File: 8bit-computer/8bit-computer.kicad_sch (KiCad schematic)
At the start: 26 parts, among them J1 USB_B

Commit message: fixing 8bit-computer schematic
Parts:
- removed C24: 10µF, Capacitor_THT:CP_Radial_D5.0mm_P2.00mm, symbol Device:CP1
- removed D2, D3, D4, D5, D6, D7, D8, D9: RED, LED_THT:LED_D5.0mm, symbol Device:LED_ALT
- added C24: 10µF, Capacitor_THT:CP_Radial_D5.0mm_P2.00mm, symbol Device:C_Polarized
- added D2, D3, D4, D5, D6, D7, D8, D9: RED, symbol Device:LED
- R10, R11, R12, R13, R14, R15, R8, R9: value 10K -> 10k
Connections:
- net A register/BUS_0: now also R15.1, D9.2 (A)
- net A register/BUS_1: now also R14.1, D8.2 (A)
- net A register/BUS_2: now also R13.1, D7.2 (A)
- net A register/BUS_3: now also R12.1, D6.2 (A)
- net A register/BUS_4: now also R11.1, D5.2 (A)
- net A register/BUS_5: now also R10.1, D4.2 (A)
- net A register/BUS_6: now also R9.1, D3.2 (A)
- net A register/BUS_7: now also R8.1, D2.2 (A)
- new net: D7.1 (K), R21.1
- new net: D6.1 (K), R20.1
- new net: D2.1 (K), R16.1
- new net: D8.1 (K), R22.1
- new net: D4.1 (K), R18.1
- new net: D3.1 (K), R17.1
- new net: D5.1 (K), R19.1
- new net: D9.1 (K), R23.1
- new net GND: C24.2, J1.4 (GND), J1.SH (Shield), R10.2, R11.2, R12.2, R13.2, R14.2, R15.2, R16.2, R17.2, R18.2, R19.2, R20.2, R21.2, R22.2, R23.2, R8.2, R9.2
- new net VCC: C24.1, J1.1 (VBUS)

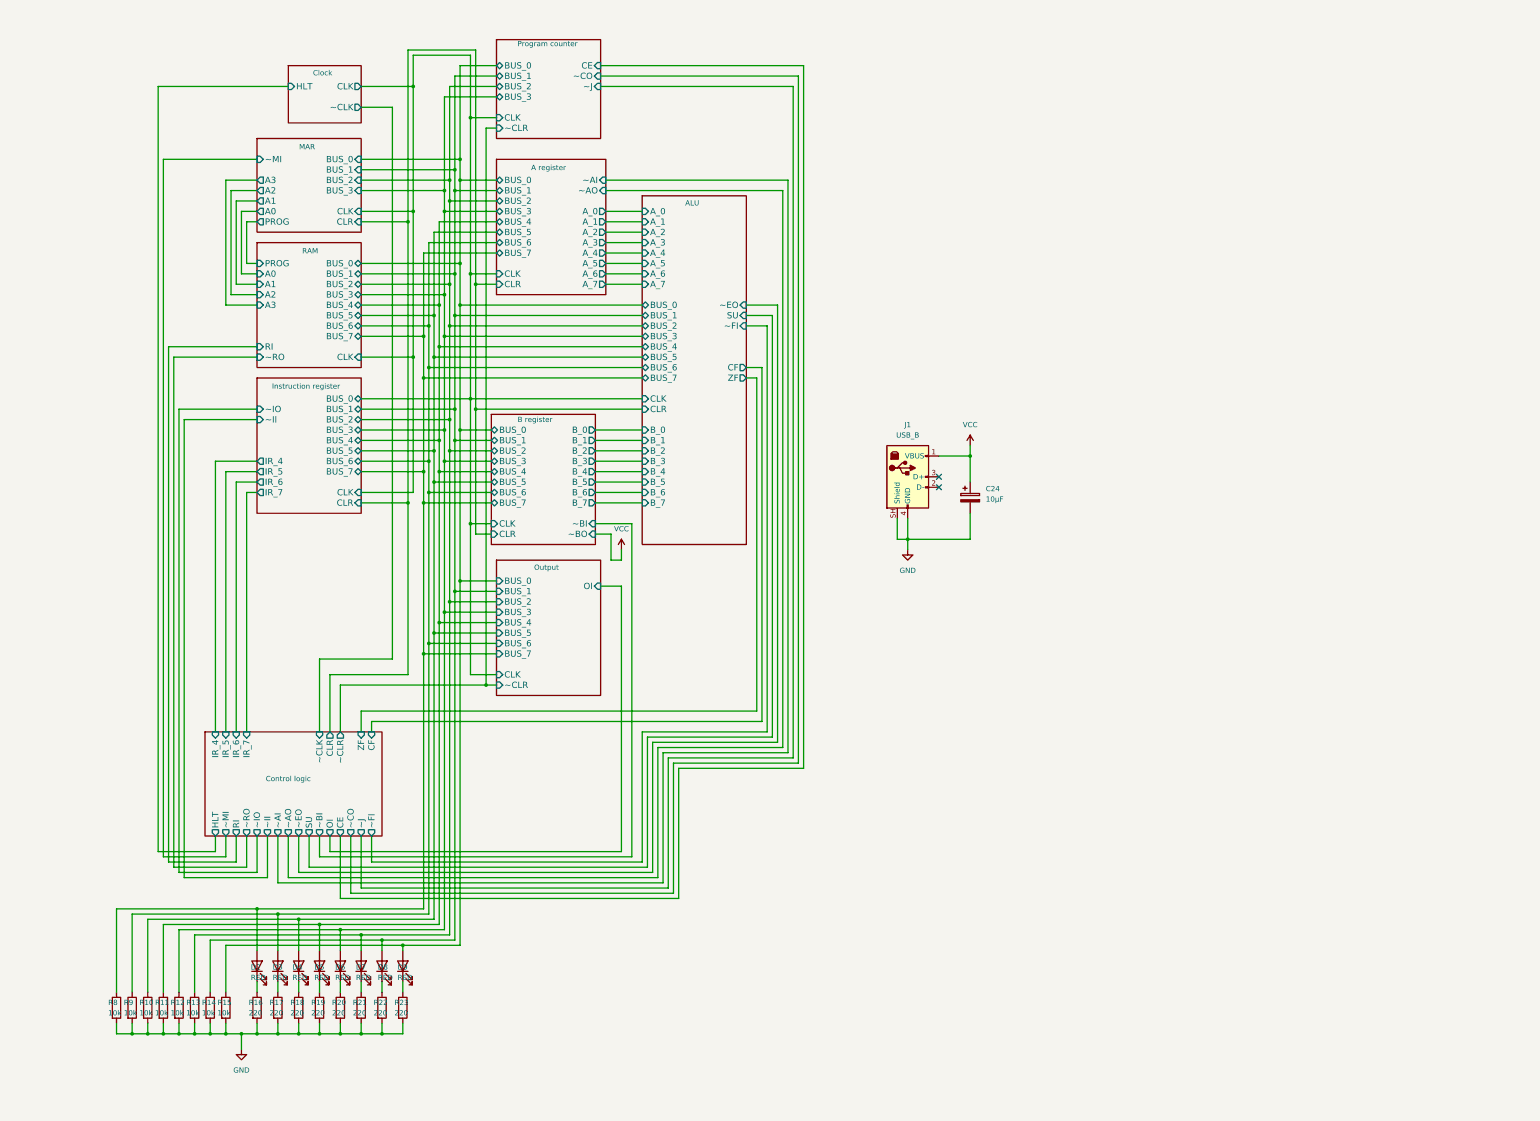
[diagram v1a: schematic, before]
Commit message: cont. drawing CPU
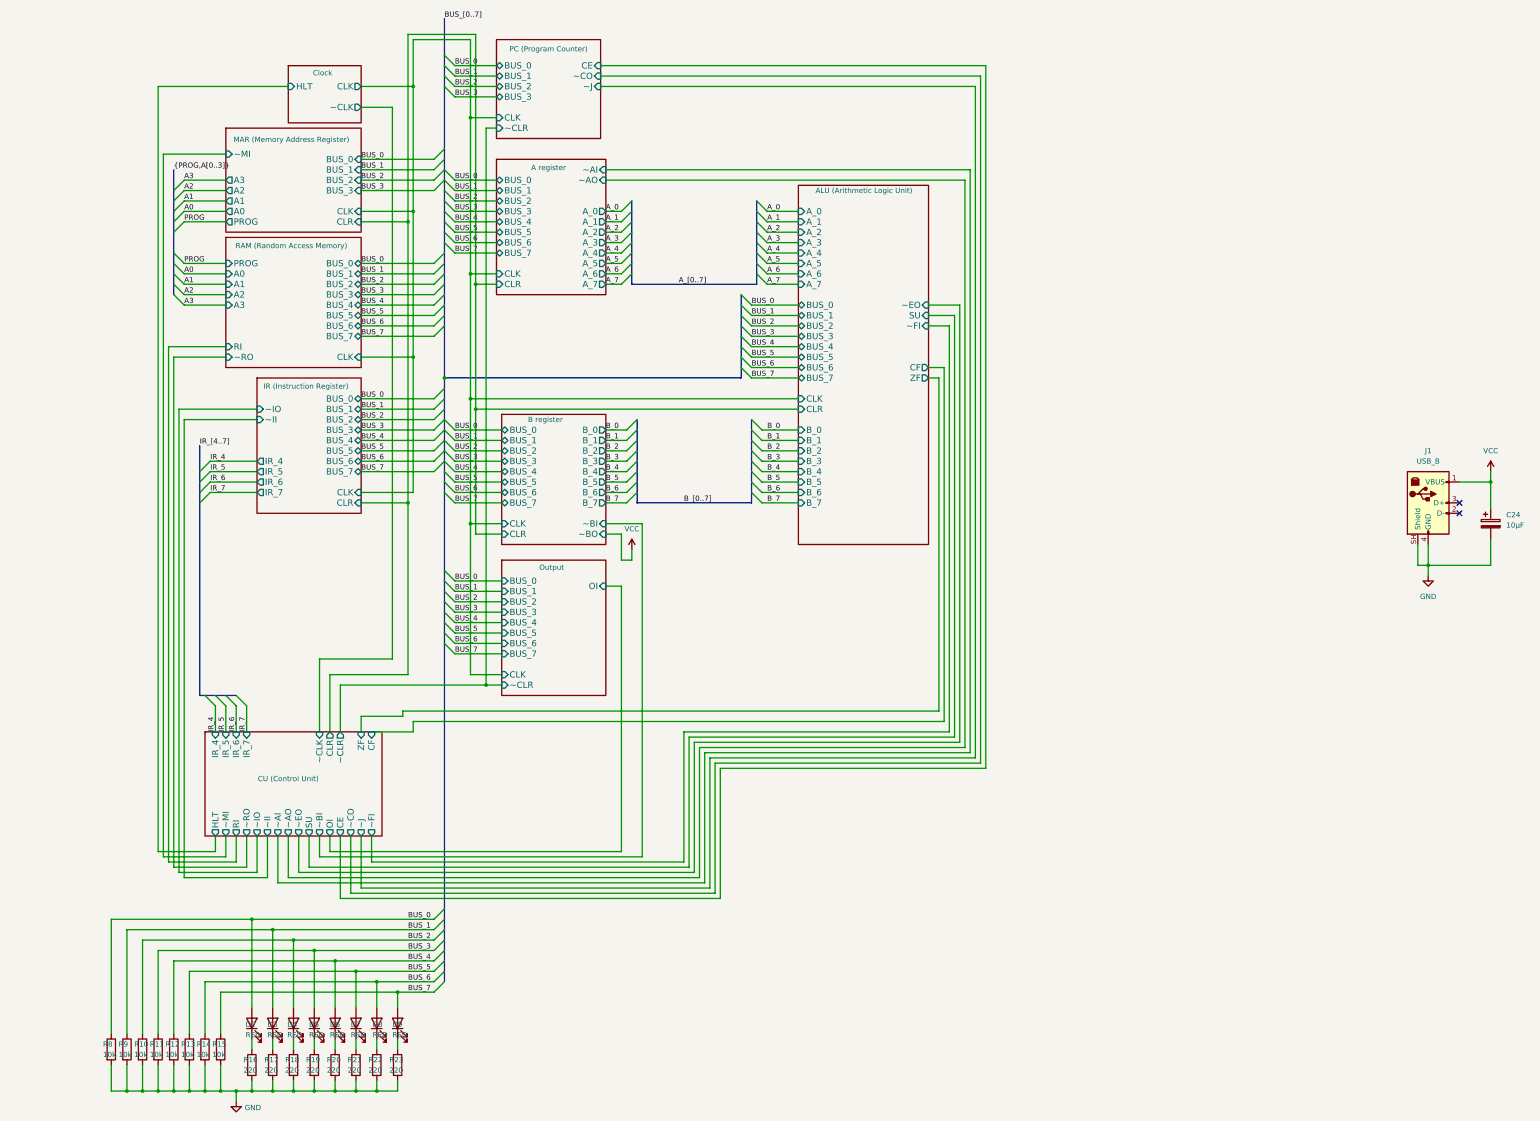
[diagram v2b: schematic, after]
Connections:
- net A register/BUS_0 renamed BUS_7
- net A register/BUS_1 renamed BUS_6
- net A register/BUS_2 renamed BUS_5
- net A register/BUS_3 renamed BUS_4
- net A register/BUS_4 renamed BUS_3
- net A register/BUS_5 renamed BUS_2
- net A register/BUS_6 renamed BUS_1
- net A register/BUS_7 renamed BUS_0
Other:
- sheet ALU renamed ALU (Arithmetic Logic Unit)
- sheet Control logic renamed CU (Control Unit)
- sheet Instruction register renamed IR (Instruction Register)
- sheet MAR renamed MAR (Memory Address Register)
- sheet Program counter renamed PC (Program Counter)
- sheet RAM renamed RAM (Random Access Memory)
- moved on the sheet: C24, D2, D3, D4, D5, D6, D7, D8, D9, J1, R10, R11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

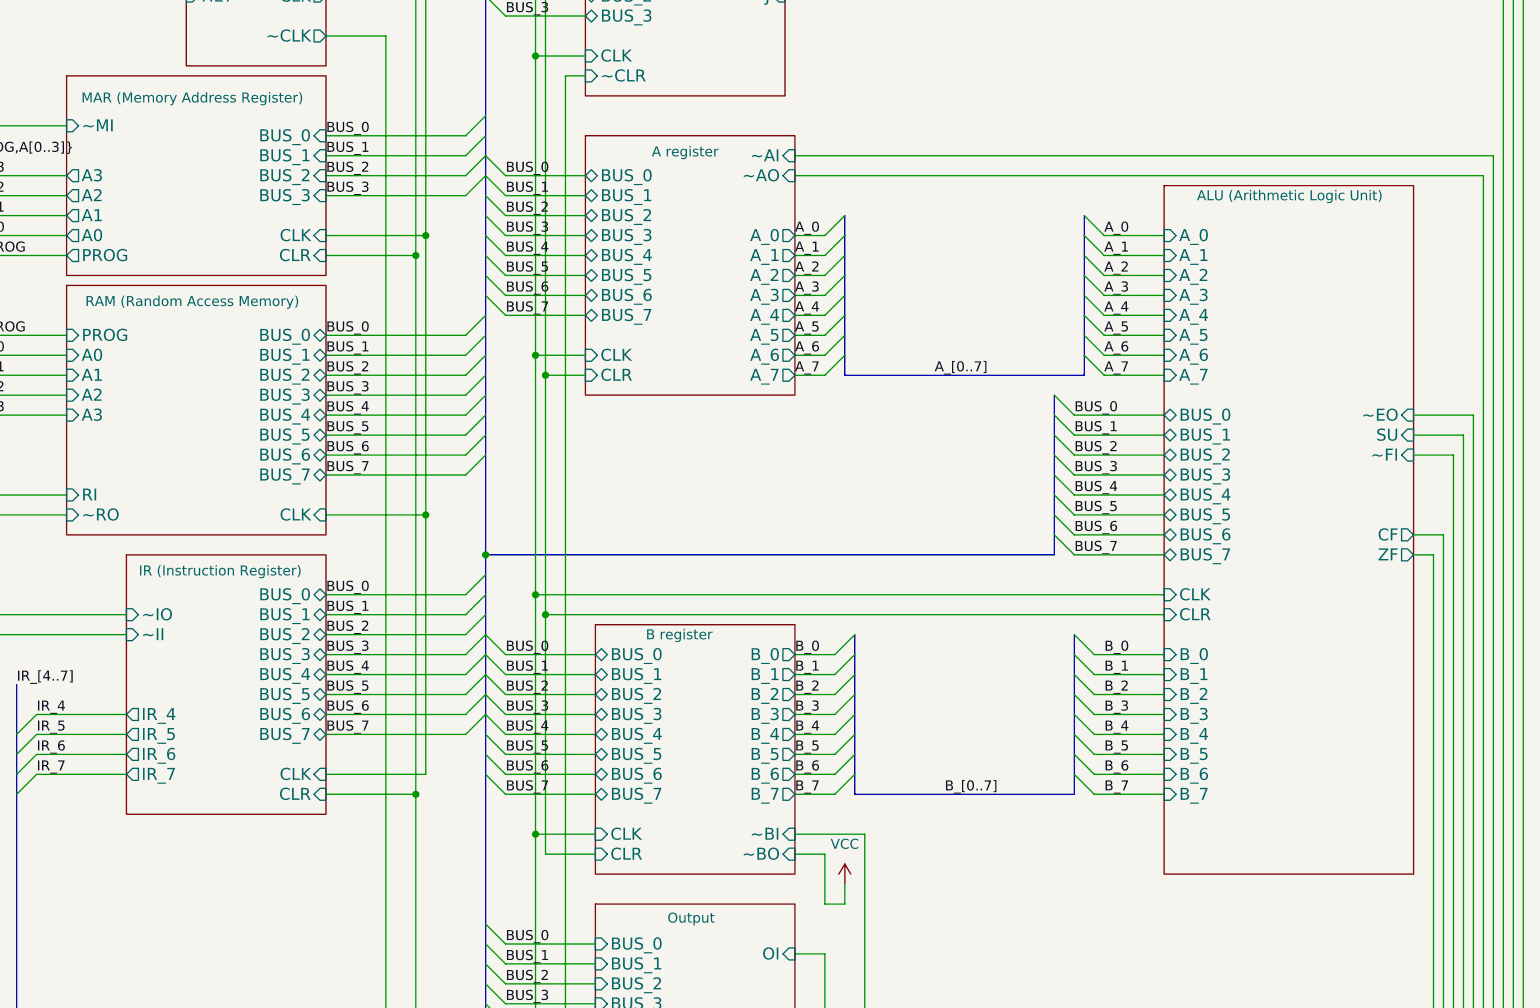
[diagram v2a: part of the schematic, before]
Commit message: using shared register schematic
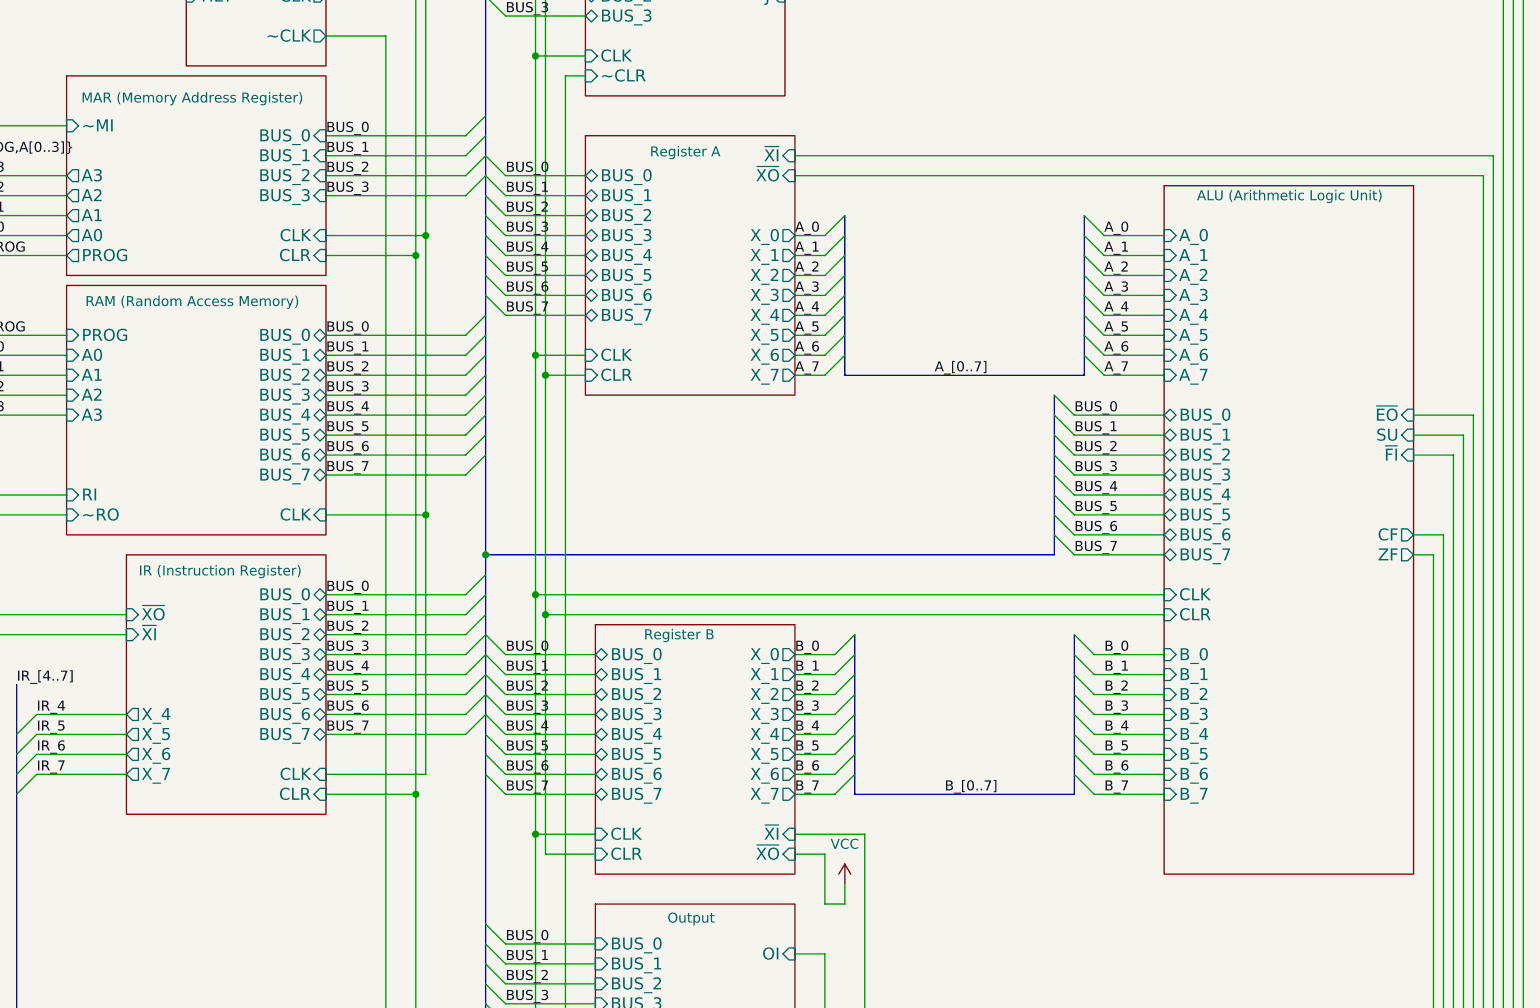
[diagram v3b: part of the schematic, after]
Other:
- sheet A register renamed Register A
- sheet B register renamed Register B
- sheet ALU (Arithmetic Logic Unit) ports: added ~{EO}, ~{FI}; removed ~EO, ~FI
- sheet IR (Instruction Register): file inst-register.kicad_sch -> register.kicad_sch
- sheet IR (Instruction Register) ports: added X_4, X_5, X_6, X_7, ~{XI}, ~{XO}; removed IR_4, IR_5, IR_6, IR_7, ~II, ~IO
- sheet Register A: file a-register.kicad_sch -> register.kicad_sch
- sheet Register A ports: added X_0, X_1, X_2, X_3, X_4, X_5, X_6, X_7, ~{XI}, ~{XO}; removed A_0, A_1, A_2, A_3, A_4, A_5, A_6, A_7, ~AI, ~AO
- sheet Register B: file b-register.kicad_sch -> register.kicad_sch
- sheet Register B ports: added X_0, X_1, X_2, X_3, X_4, X_5, X_6, X_7, ~{XI}, ~{XO}; removed B_0, B_1, B_2, B_3, B_4, B_5, B_6, B_7, ~BI, ~BO
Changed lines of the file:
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@@
 			(color 0 0 0 0)
 		)
-		(property "Sheetname" "B register"
+		(property "Sheetname" "Register B"
 			(at 135.128 113.03 0)
 			(show_name no)
@@
 			)
 		)
-		(property "Sheetfile" "b-register.kicad_sch"
+		(property "Sheetfile" "register.kicad_sch"
 			(at 136.398 115.824 0)
 			(hide yes)
@@
 			)
 		)
-		(pin "B_0" output
+		(pin "X_0" output
 			(at 149.86 115.57 0)
 			(effects
@@
 			)
 		)
-		(pin "B_1" output
+		(pin "X_1" output
 			(at 149.86 118.11 0)
 			(effects
@@
 			)
 		)
-		(pin "B_2" output
+		(pin "X_2" output
 			(at 149.86 120.65 0)
 			(effects
@@
 			)
 		)
-		(pin "B_3" output
+		(pin "X_3" output
 			(at 149.86 123.19 0)
 			(effects
@@
 			)
 		)
-		(pin "B_4" output
+		(pin "X_4" output
 			(at 149.86 125.73 0)
 			(effects
@@
 			)
 		)
-		(pin "B_5" output
+		(pin "X_5" output
 			(at 149.86 128.27 0)
 			(effects
@@
 			)
 		)
-		(pin "B_6" output
+		(pin "X_6" output
 			(at 149.86 130.81 0)
 			(effects
@@
 			)
 		)
-		(pin "B_7" output
+		(pin "X_7" output
 			(at 149.86 133.35 0)
 			(effects
@@
 			)
 		)
-		(pin "~BO" input
+		(pin "~{XO}" input
 			(at 149.86 140.97 0)
 			(effects
@@
 			)
 		)
-		(pin "~BI" input
+		(pin "~{XI}" input
 			(at 149.86 138.43 0)
 			(effects
@@
 			(project "8bit-computer"
 				(path "/ad4ae7b4-c6cb-482b-83a8-8fafb97d09a4"
-					(page "")
+					(page "#")
 				)
 			)
@@
 			(project "8bit-computer"
 				(path "/ad4ae7b4-c6cb-482b-83a8-8fafb97d09a4"
-					(page "")
+					(page "#")
 				)
 			)
@@
 			(project "8bit-computer"
 				(path "/ad4ae7b4-c6cb-482b-83a8-8fafb97d09a4"
-					(page "")
+					(page "#")
 				)
 			)
@@
 			(project "8bit-computer"
 				(path "/ad4ae7b4-c6cb-482b-83a8-8fafb97d09a4"
-					(page "")
+					(page "#")
 				)
 			)
@@
 			)
 		)
-		(property "Sheetfile" "inst-register.kicad_sch"
+		(property "Sheetfile" "register.kicad_sch"
 			(at 76.962 119.38 0)
 			(hide yes)
@@
 			)
 		)
-		(pin "IR_4" output
+		(pin "X_4" output
 			(at 64.77 123.19 180)
 			(effects
@@
 			)
 		)
-		(pin "IR_5" output
+		(pin "X_5" output
 			(at 64.77 125.73 180)
 			(effects
@@
 			)
 		)
-		(pin "IR_6" output
+		(pin "X_6" output
 			(at 64.77 128.27 180)
 			(effects
@@
 			)
 		)
-		(pin "IR_7" output
+		(pin "X_7" output
 			(at 64.77 130.81 180)
 			(effects
@@
 			)
 		)
-		(pin "~IO" input
+		(pin "~{XO}" input
 			(at 64.77 110.49 180)
 			(effects
@@
 			)
 		)
-		(pin "~II" input
+		(pin "~{XI}" input
 			(at 64.77 113.03 180)
 			(effects
@@
 			(project "8bit-computer"
 				(path "/ad4ae7b4-c6cb-482b-83a8-8fafb97d09a4"
-					(page "")
+					(page "#")
 				)
 			)
@@
 			(project "8bit-computer"
 				(path "/ad4ae7b4-c6cb-482b-83a8-8fafb97d09a4"
-					(page "")
+					(page "#")
 				)
 			)
@@
 			(project "8bit-computer"
 				(path "/ad4ae7b4-c6cb-482b-83a8-8fafb97d09a4"
-					(page "")
+					(page "#")
 				)
 			)
@@
 			)
 		)
-		(pin "~EO" input
+		(pin "~{EO}" input
 			(at 228.6 85.09 0)
 			(effects
@@
 			)
 		)
-		(pin "~FI" input
+		(pin "~{FI}" input
 			(at 228.6 90.17 0)
 			(effects
@@
 			(project "8bit-computer"
 				(path "/ad4ae7b4-c6cb-482b-83a8-8fafb97d09a4"
-					(page "")
+					(page "#")
 				)
 			)
@@
 			(project "8bit-computer"
 				(path "/ad4ae7b4-c6cb-482b-83a8-8fafb97d09a4"
-					(page "")
+					(page "#")
 				)
 			)
@@
 			(color 0 0 0 0)
 		)
-		(property "Sheetname" "A register"
+		(property "Sheetname" "Register A"
 			(at 135.89 51.562 0)
 			(show_name no)
@@
 			)
 		)
-		(property "Sheetfile" "a-register.kicad_sch"
+		(property "Sheetfile" "register.kicad_sch"
 			(at 136.652 54.102 0)
 			(hide yes)
@@
 			)
 		)
-		(pin "A_7" output
+		(pin "X_7" output
 			(at 149.86 80.01 0)
 			(effects
@@
 			)
 		)
-		(pin "A_6" output
+		(pin "X_6" output
 			(at 149.86 77.47 0)
 			(effects
@@
 			)
 		)
-		(pin "A_5" output
+		(pin "X_5" output
 			(at 149.86 74.93 0)
 			(effects
@@
 			)
 		)
-		(pin "A_4" output
+		(pin "X_4" output
 			(at 149.86 72.39 0)
 			(effects
@@
 			)
 		)
-		(pin "A_3" output
+		(pin "X_3" output
 			(at 149.86 69.85 0)
 			(effects
@@
 			)
 		)
-		(pin "A_2" output
+		(pin "X_2" output
 			(at 149.86 67.31 0)
 			(effects
@@
 			)
 		)
-		(pin "A_1" output
+		(pin "X_1" output
 			(at 149.86 64.77 0)
 			(effects
@@
 			)
 		)
-		(pin "A_0" output
+		(pin "X_0" output
 			(at 149.86 62.23 0)
 			(effects
@@
 			)
 		)
-		(pin "~AI" input
+		(pin "~{XI}" input
 			(at 149.86 52.07 0)
 			(effects
@@
 			)
 		)
-		(pin "~AO" input
+		(pin "~{XO}" input
 			(at 149.86 54.61 0)
 			(effects
@@
 			(project "8bit-computer"
 				(path "/ad4ae7b4-c6cb-482b-83a8-8fafb97d09a4"
-					(page "")
-				)
-			)
+					(page "#")
+				)
+			)

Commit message: cont. 8bit schematics
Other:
- sheet CU (Control Unit) ports: added ~{AI}, ~{AO}, ~{BI}, ~{CLK}, ~{CLR}, ~{CO}, ~{EO}, ~{FI}, ~{II}, ~{IO}, ~{J}, ~{MI}, ~{RO}; removed ~AI, ~AO, ~BI, ~CLK, ~CLR, ~CO, ~EO, ~FI, ~II, ~IO, ~J, ~MI, ~RO
- sheet Clock ports: added ~{CLK}; removed ~CLK
- sheet PC (Program Counter) ports: added ~{CO}, ~{J}; removed ~CO, ~J
- title: (none) -> 8 Bit Computer
